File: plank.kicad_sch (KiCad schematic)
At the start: 14 parts, among them SW1 SW_Push, U1 ATmega32U4-A, Y1 16MHz

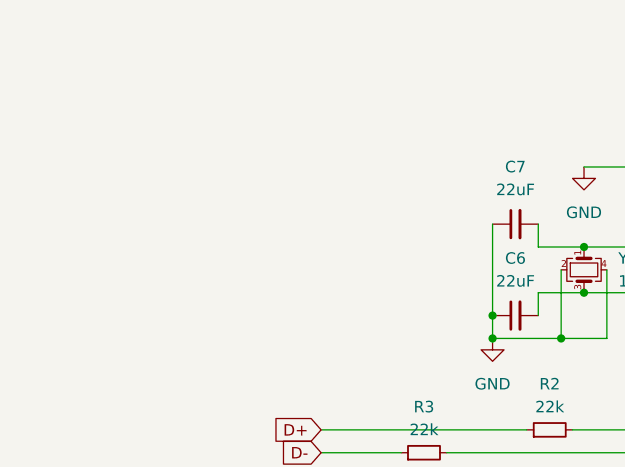
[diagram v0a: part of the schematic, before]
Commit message: Added USB Molex
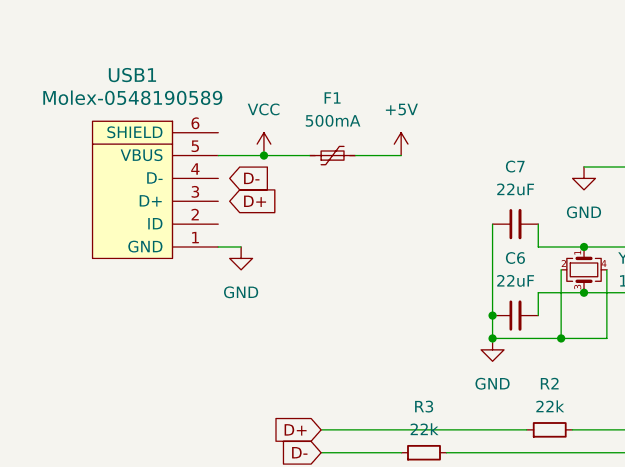
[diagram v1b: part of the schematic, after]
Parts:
- added F1: 500mA, symbol Device:Polyfuse_Small
- added USB1: Molex-0548190589, symbol random-keyboard-parts:Molex-0548190589
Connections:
- net +5V: now also F1.2
- net GND: now also USB1.1 (GND)
- new net VCC: F1.1, USB1.5 (VBUS)
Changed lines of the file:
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@@
   (junction (at 82.55 57.15) (diameter 0) (color 0 0 0 0)
+  )
+  (junction (at 57.15 39.37) (diameter 0) (color 0 0 0 0)
   )
   (junction (at 124.46 128.27) (diameter 0) (color 0 0 0 0)
@@
     (stroke (width 0) (type default))
   )
+  (wire (pts (xy 67.31 39.37) (xy 72.39 39.37))
+    (stroke (width 0) (type default))
+  )
   (wire (pts (xy 92.71 54.61) (xy 111.76 54.61))
     (stroke (width 0) (type default))
@@
     (stroke (width 0) (type default))
   )
+  (wire (pts (xy 52.07 49.53) (xy 54.61 49.53))
+    (stroke (width 0) (type default))
+  )
   (wire (pts (xy 99.06 40.64) (xy 92.71 40.64))
     (stroke (width 0) (type default))
@@
     (stroke (width 0) (type default))
   )
+  (wire (pts (xy 57.15 39.37) (xy 62.23 39.37))
+    (stroke (width 0) (type default))
+  )
   (wire (pts (xy 64.77 101.6) (xy 77.47 101.6))
     (stroke (width 0) (type default))
@@
   )
   (wire (pts (xy 90.17 106.68) (xy 102.87 106.68))
+    (stroke (width 0) (type default))
+  )
+  (wire (pts (xy 52.07 39.37) (xy 57.15 39.37))
     (stroke (width 0) (type default))
   )
@@
     )
   )
+  (global_label "D+" (shape input) (at 53.34 44.45 0) (fields_autoplaced)
+    (effects (font (size 1.27 1.27)) (justify left))
+    (property "Intersheetrefs" "${INTERSHEET_REFS}" (at 59.1676 44.45 0)
+      (effects (font (size 1.27 1.27)) (justify left) hide)
+    )
+  )
+  (global_label "D-" (shape input) (at 53.34 41.91 0) (fields_autoplaced)
+    (effects (font (size 1.27 1.27)) (justify left))
+    (property "Intersheetrefs" "${INTERSHEET_REFS}" (at 59.1676 41.91 0)
+      (effects (font (size 1.27 1.27)) (justify left) hide)
+    )
+  )
   (global_label "D-" (shape input) (at 63.5 72.39 180) (fields_autoplaced)
     (effects (font (size 1.27 1.27)) (justify right))
@@
     )
   )
+  (symbol (lib_id "power:+5V") (at 72.39 39.37 0) (unit 1)
+    (in_bom yes) (on_board yes) (dnp no) (fields_autoplaced)
+    (property "Reference" "#PWR012" (at 72.39 43.18 0)
+      (effects (font (size 1.27 1.27)) hide)
+    )
+    (property "Value" "+5V" (at 72.39 34.29 0)
+      (effects (font (size 1.27 1.27)))
+    )
+    (property "Footprint" "" (at 72.39 39.37 0)
+      (effects (font (size 1.27 1.27)) hide)
+    )
+    (property "Datasheet" "" (at 72.39 39.37 0)
+      (effects (font (size 1.27 1.27)) hide)
+    )
+    (pin "1")
+    (instances
+      (project "plank"
+        (path "/56e11f07-968c-4d42-931a-9a646d695afe"
+          (reference "#PWR012") (unit 1)
+        )
+      )
+    )
+  )
   (symbol (lib_id "Device:C_Small") (at 77.47 104.14 0) (unit 1)
     (in_bom yes) (on_board yes) (dnp no) (fields_autoplaced)
@@
     )
   )
+  (symbol (lib_id "random-keyboard-parts:Molex-0548190589") (at 44.45 44.45 90) (unit 1)
+    (in_bom yes) (on_board yes) (dnp no) (fields_autoplaced)
+    (property "Reference" "USB1" (at 42.545 30.48 90)
+      (effects (font (size 1.524 1.524)))
+    )
+    (property "Value" "Molex-0548190589" (at 42.545 33.02 90)
+      (effects (font (size 1.524 1.524)))
+    )
+    (property "Footprint" "" (at 44.45 44.45 0)
+      (effects (font (size 1.524 1.524)) hide)
+    )
+    (property "Datasheet" "" (at 44.45 44.45 0)
+      (effects (font (size 1.524 1.524)) hide)
+    )
+    (pin "6")
+    (pin "1")
+    (pin "2")
+    (pin "3")
+    (pin "4")
+    (pin "5")
+    (instances
+      (project "plank"
+        (path "/56e11f07-968c-4d42-931a-9a646d695afe"
+          (reference "USB1") (unit 1)
+        )
+      )
+    )
+  )
   (symbol (lib_id "power:GND") (at 101.6 85.09 0) (unit 1)
     (in_bom yes) (on_board yes) (dnp no) (fields_autoplaced)
@@
     )
   )
+  (symbol (lib_id "power:VCC") (at 57.15 39.37 0) (unit 1)
+    (in_bom yes) (on_board yes) (dnp no) (fields_autoplaced)
+    (property "Reference" "#PWR011" (at 57.15 43.18 0)
+      (effects (font (size 1.27 1.27)) hide)
+    )
+    (property "Value" "VCC" (at 57.15 34.29 0)
+      (effects (font (size 1.27 1.27)))
+    )
+    (property "Footprint" "" (at 57.15 39.37 0)
+      (effects (font (size 1.27 1.27)) hide)
+    )
+    (property "Datasheet" "" (at 57.15 39.37 0)
+      (effects (font (size 1.27 1.27)) hide)
+    )
+    (pin "1")
+    (instances
+      (project "plank"
+        (path "/56e11f07-968c-4d42-931a-9a646d695afe"
+          (reference "#PWR011") (unit 1)
+        )
+      )
+    )
+  )
   (symbol (lib_id "Device:R_Small") (at 110.49 35.56 0) (unit 1)
     (in_bom yes) (on_board yes) (dnp no) (fields_autoplaced)
@@
         (path "/56e11f07-968c-4d42-931a-9a646d695afe"
           (reference "R4") (unit 1)
+        )
+      )
+    )
+  )
+  (symbol (lib_id "power:GND") (at 54.61 49.53 0) (unit 1)
+    (in_bom yes) (on_board yes) (dnp no) (fields_autoplaced)
+    (property "Reference" "#PWR013" (at 54.61 55.88 0)
+      (effects (font (size 1.27 1.27)) hide)
+    )
+    (property "Value" "GND" (at 54.61 54.61 0)
+      (effects (font (size 1.27 1.27)))
+    )
+    (property "Footprint" "" (at 54.61 49.53 0)
+      (effects (font (size 1.27 1.27)) hide)
+    )
+    (property "Datasheet" "" (at 54.61 49.53 0)
+      (effects (font (size 1.27 1.27)) hide)
+    )
+    (pin "1")
+    (instances
+      (project "plank"
+        (path "/56e11f07-968c-4d42-931a-9a646d695afe"
+          (reference "#PWR013") (unit 1)
         )
       )
@@
         )
       )
+    )
+  )
+  (symbol (lib_id "Device:Polyfuse_Small") (at 64.77 39.37 90) (unit 1)
+    (in_bom yes) (on_board yes) (dnp no) (fields_autoplaced)
+    (property "Reference" "F1" (at 64.77 33.02 90)
+      (effects (font (size 1.27 1.27)))
+    )
+    (property "Value" "500mA" (at 64.77 35.56 90)
+      (effects (font (size 1.27 1.27)))
+    )
+    (property "Footprint" "" (at 69.85 38.1 0)
+      (effects (font (size 1.27 1.27)) (justify left) hide)
+    )
+    (property "Datasheet" "~" (at 64.77 39.37 0)
+      (effects (font (size 1.27 1.27)) hide)
+    )
+    (pin "2")
+    (pin "1")
+    (instances
+      (project "plank"
+        (path "/56e11f07-968c-4d42-931a-9a646d695afe"
+          (reference "F1") (unit 1)
+        )
+      )

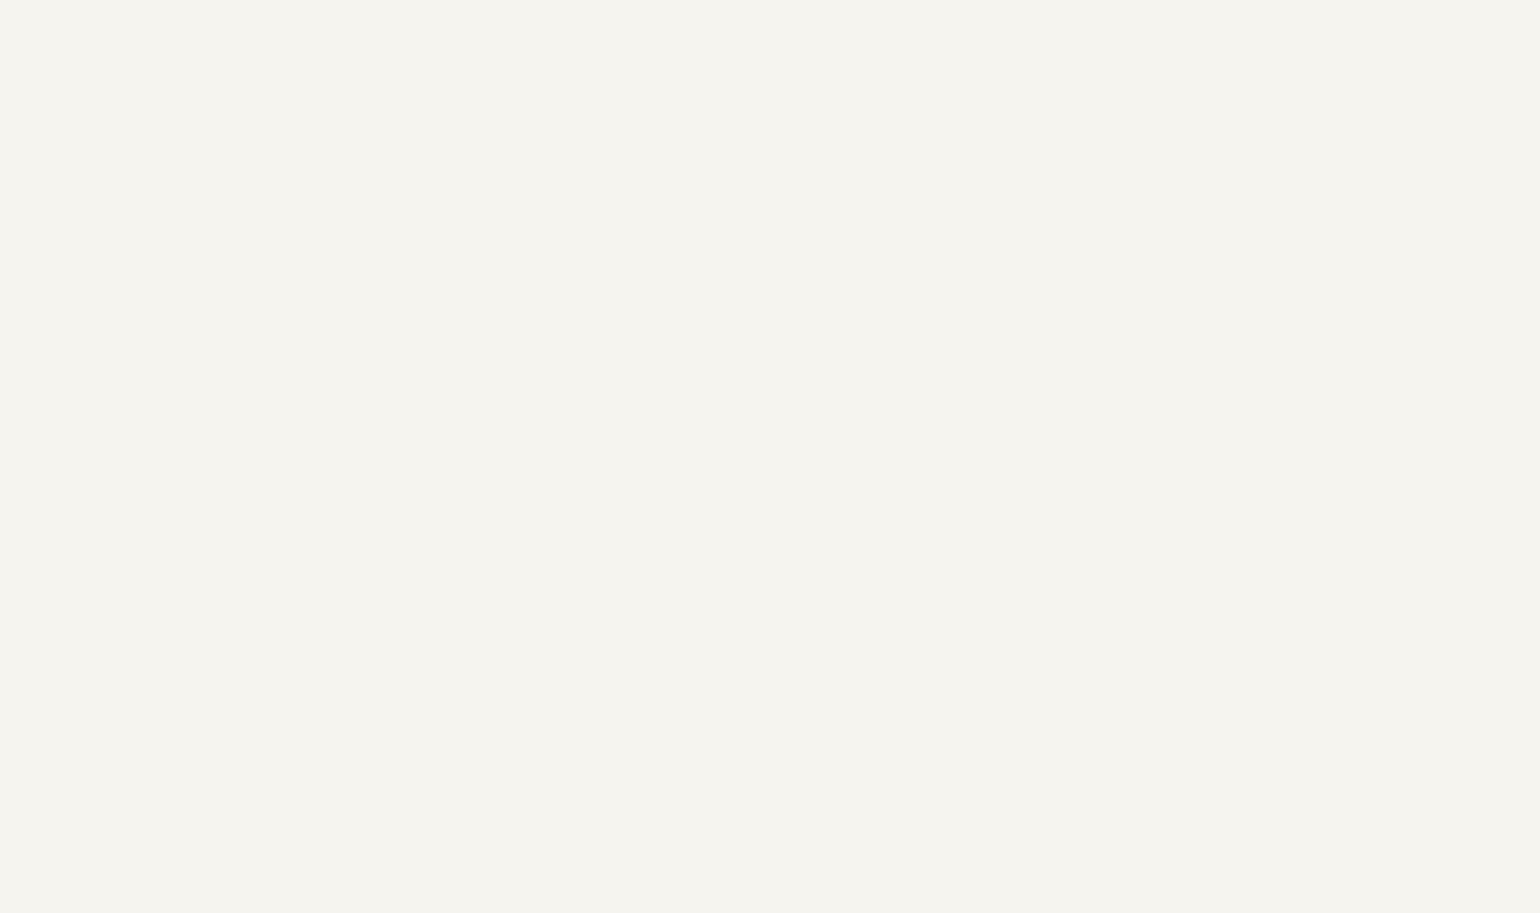
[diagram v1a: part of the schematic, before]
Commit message: Added switch matrix
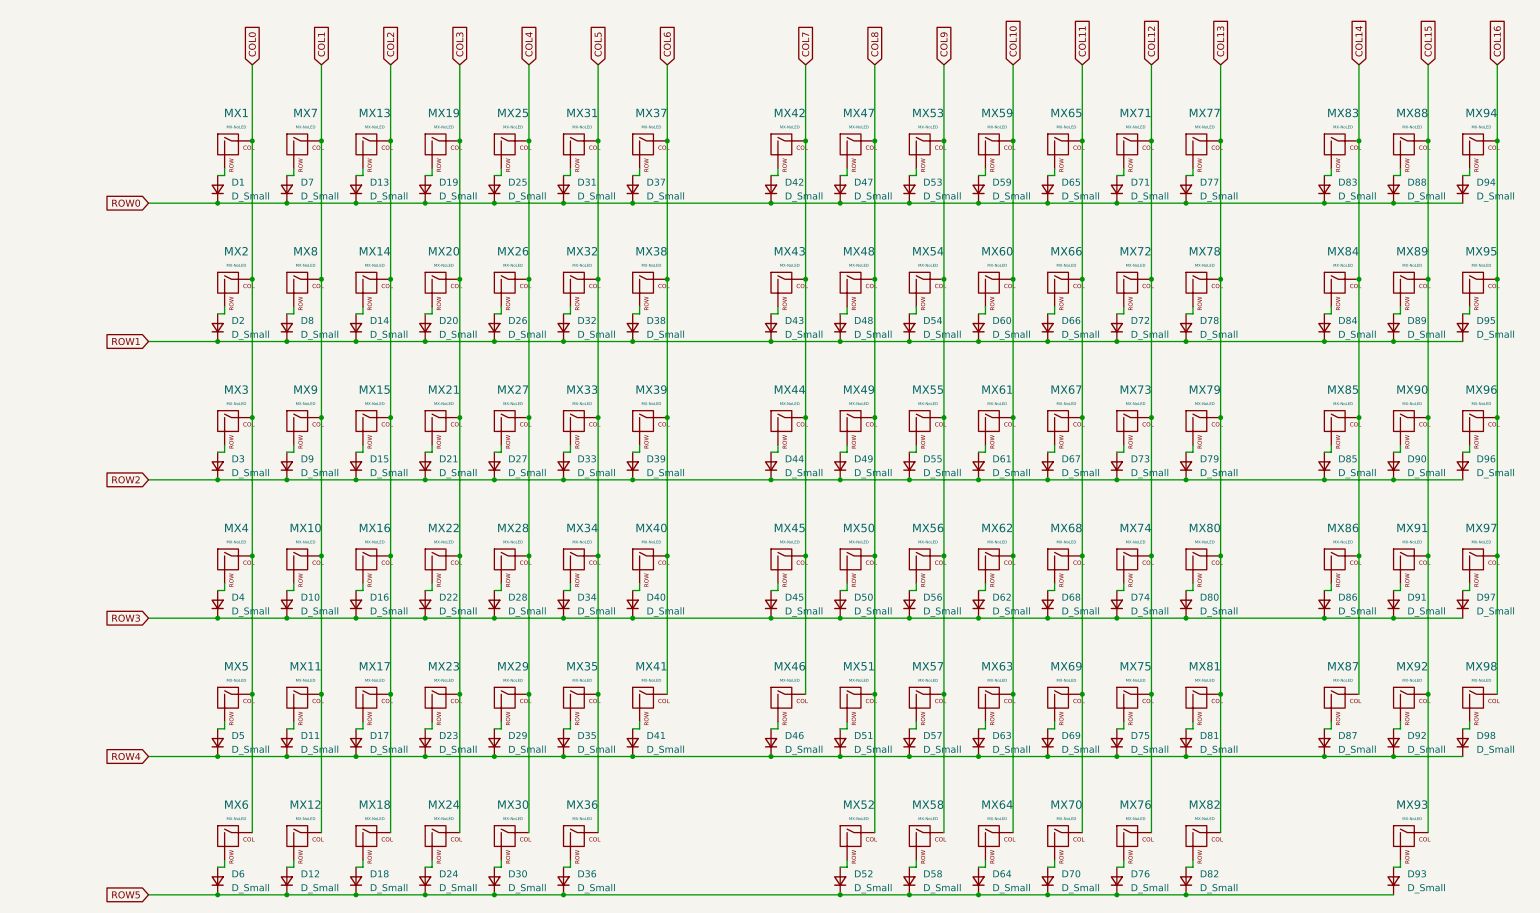
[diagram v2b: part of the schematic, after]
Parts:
- added D1, D10, D11, D12, D13, D14, D15, D16, D17, D18, D19, D2, D20, D21, D22, D23, D24, D25, D26, D27, D28, D29, D3, D30, D31, D32, D33, D34, D35, D36, D37, D38, D39, D4, D40, D41, D42, D43, D44, D45, D46, D47, D48, D49, D5, D50, D51, D52, D53, D54, D55, D56, D57, D58, D59, D6, D60, D61, D62, D63, D64, D65, D66, D67, D68, D69, D7, D70, D71, D72, D73, D74, D75, D76, D77, D78, D79, D8, D80, D81, D82, D83, D84, D85, D86, D87, D88, D89, D9, D90, D91, D92, D93, D94, D95, D96, D97, D98: D_Small, symbol Device:D_Small
- added MX1, MX10, MX11, MX12, MX13, MX14, MX15, MX16, MX17, MX18, MX19, MX2, MX20, MX21, MX22, MX23, MX24, MX25, MX26, MX27, MX28, MX29, MX3, MX30, MX31, MX32, MX33, MX34, MX35, MX36, MX37, MX38, MX39, MX4, MX40, MX41, MX42, MX43, MX44, MX45, MX46, MX47, MX48, MX49, MX5, MX50, MX51, MX52, MX53, MX54, MX55, MX56, MX57, MX58, MX59, MX6, MX60, MX61, MX62, MX63, MX64, MX65, MX66, MX67, MX68, MX69, MX7, MX70, MX71, MX72, MX73, MX74, MX75, MX76, MX77, MX78, MX79, MX8, MX80, MX81, MX82, MX83, MX84, MX85, MX86, MX87, MX88, MX89, MX9, MX90, MX91, MX92, MX93, MX94, MX95, MX96, MX97, MX98: MX-NoLED, symbol MX_Alps_Hybrid:MX-NoLED
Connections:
- new net: D26.2 (A), MX26.2 (ROW)
- new net: D72.2 (A), MX72.2 (ROW)
- new net: D75.2 (A), MX75.2 (ROW)
- new net: D35.2 (A), MX35.2 (ROW)
- new net: D70.2 (A), MX70.2 (ROW)
- new net: D5.2 (A), MX5.2 (ROW)
- new net: D32.2 (A), MX32.2 (ROW)
- new net: D29.2 (A), MX29.2 (ROW)
- new net: D3.2 (A), MX3.2 (ROW)
- new net: D74.2 (A), MX74.2 (ROW)
- new net: D45.2 (A), MX45.2 (ROW)
- new net: D39.2 (A), MX39.2 (ROW)
- new net: D47.2 (A), MX47.2 (ROW)
- new net: D44.2 (A), MX44.2 (ROW)
- new net: D20.2 (A), MX20.2 (ROW)
- new net: D58.2 (A), MX58.2 (ROW)
- new net: D55.2 (A), MX55.2 (ROW)
- new net: D84.2 (A), MX84.2 (ROW)
- new net: D77.2 (A), MX77.2 (ROW)
- new net: D13.2 (A), MX13.2 (ROW)
- new net: D15.2 (A), MX15.2 (ROW)
- new net: D79.2 (A), MX79.2 (ROW)
- new net: D63.2 (A), MX63.2 (ROW)
- new net: D18.2 (A), MX18.2 (ROW)
- new net: D95.2 (A), MX95.2 (ROW)
- new net: D80.2 (A), MX80.2 (ROW)
- new net: D21.2 (A), MX21.2 (ROW)
- new net: D66.2 (A), MX66.2 (ROW)
- new net: D91.2 (A), MX91.2 (ROW)
- new net: D98.2 (A), MX98.2 (ROW)
- new net: D33.2 (A), MX33.2 (ROW)
- new net: D82.2 (A), MX82.2 (ROW)
- new net: D59.2 (A), MX59.2 (ROW)
- new net: D62.2 (A), MX62.2 (ROW)
- new net: D50.2 (A), MX50.2 (ROW)
- new net: D31.2 (A), MX31.2 (ROW)
- new net: D83.2 (A), MX83.2 (ROW)
- new net: D52.2 (A), MX52.2 (ROW)
- new net: D12.2 (A), MX12.2 (ROW)
- new net: D49.2 (A), MX49.2 (ROW)
- new net: D81.2 (A), MX81.2 (ROW)
- new net: D53.2 (A), MX53.2 (ROW)
- new net: D19.2 (A), MX19.2 (ROW)
- new net: D4.2 (A), MX4.2 (ROW)
- new net: D89.2 (A), MX89.2 (ROW)
- new net: D92.2 (A), MX92.2 (ROW)
- new net: D96.2 (A), MX96.2 (ROW)
- new net: D67.2 (A), MX67.2 (ROW)
- new net: D14.2 (A), MX14.2 (ROW)
- new net: D90.2 (A), MX90.2 (ROW)
- new net: D24.2 (A), MX24.2 (ROW)
- new net: D54.2 (A), MX54.2 (ROW)
- new net: D34.2 (A), MX34.2 (ROW)
- new net: D7.2 (A), MX7.2 (ROW)
- new net: D11.2 (A), MX11.2 (ROW)
- new net: D37.2 (A), MX37.2 (ROW)
- new net: D42.2 (A), MX42.2 (ROW)
- new net: D23.2 (A), MX23.2 (ROW)
- new net: D36.2 (A), MX36.2 (ROW)
- new net: D97.2 (A), MX97.2 (ROW)
- new net: D51.2 (A), MX51.2 (ROW)
- new net: D25.2 (A), MX25.2 (ROW)
- new net: D86.2 (A), MX86.2 (ROW)
- new net: D17.2 (A), MX17.2 (ROW)
- new net: D30.2 (A), MX30.2 (ROW)
- new net: D28.2 (A), MX28.2 (ROW)
- new net: D46.2 (A), MX46.2 (ROW)
- new net: D94.2 (A), MX94.2 (ROW)
- new net: D57.2 (A), MX57.2 (ROW)
- new net: D88.2 (A), MX88.2 (ROW)
- new net: D27.2 (A), MX27.2 (ROW)
- new net: D48.2 (A), MX48.2 (ROW)
- new net: D9.2 (A), MX9.2 (ROW)
- new net: D64.2 (A), MX64.2 (ROW)
- new net: D8.2 (A), MX8.2 (ROW)
- new net: D73.2 (A), MX73.2 (ROW)
- new net: D76.2 (A), MX76.2 (ROW)
- new net: D6.2 (A), MX6.2 (ROW)
- new net: D2.2 (A), MX2.2 (ROW)
- new net: D38.2 (A), MX38.2 (ROW)
- new net: D10.2 (A), MX10.2 (ROW)
- new net: D65.2 (A), MX65.2 (ROW)
- new net: D71.2 (A), MX71.2 (ROW)
- new net: D60.2 (A), MX60.2 (ROW)
- new net: D61.2 (A), MX61.2 (ROW)
- new net: D43.2 (A), MX43.2 (ROW)
- new net: D69.2 (A), MX69.2 (ROW)
- new net: D87.2 (A), MX87.2 (ROW)
- new net: D93.2 (A), MX93.2 (ROW)
- new net: D41.2 (A), MX41.2 (ROW)
- new net: D22.2 (A), MX22.2 (ROW)
- new net: D78.2 (A), MX78.2 (ROW)
- new net: D1.2 (A), MX1.2 (ROW)
- new net: D40.2 (A), MX40.2 (ROW)
- new net: D56.2 (A), MX56.2 (ROW)
- new net: D68.2 (A), MX68.2 (ROW)
- new net: D85.2 (A), MX85.2 (ROW)
- new net: D16.2 (A), MX16.2 (ROW)
- new net COL0: MX1.1 (COL), MX2.1 (COL), MX3.1 (COL), MX4.1 (COL), MX5.1 (COL), MX6.1 (COL)
- new net COL1: MX10.1 (COL), MX11.1 (COL), MX12.1 (COL), MX7.1 (COL), MX8.1 (COL), MX9.1 (COL)
- new net COL10: MX59.1 (COL), MX60.1 (COL), MX61.1 (COL), MX62.1 (COL), MX63.1 (COL), MX64.1 (COL)
- new net COL11: MX65.1 (COL), MX66.1 (COL), MX67.1 (COL), MX68.1 (COL), MX69.1 (COL), MX70.1 (COL)
- new net COL12: MX71.1 (COL), MX72.1 (COL), MX73.1 (COL), MX74.1 (COL), MX75.1 (COL), MX76.1 (COL)
- new net COL13: MX77.1 (COL), MX78.1 (COL), MX79.1 (COL), MX80.1 (COL), MX81.1 (COL), MX82.1 (COL)
- new net COL14: MX83.1 (COL), MX84.1 (COL), MX85.1 (COL), MX86.1 (COL), MX87.1 (COL)
- new net COL15: MX88.1 (COL), MX89.1 (COL), MX90.1 (COL), MX91.1 (COL), MX92.1 (COL), MX93.1 (COL)
- new net COL16: MX94.1 (COL), MX95.1 (COL), MX96.1 (COL), MX97.1 (COL), MX98.1 (COL)
- new net COL2: MX13.1 (COL), MX14.1 (COL), MX15.1 (COL), MX16.1 (COL), MX17.1 (COL), MX18.1 (COL)
- new net COL3: MX19.1 (COL), MX20.1 (COL), MX21.1 (COL), MX22.1 (COL), MX23.1 (COL), MX24.1 (COL)
- new net COL4: MX25.1 (COL), MX26.1 (COL), MX27.1 (COL), MX28.1 (COL), MX29.1 (COL), MX30.1 (COL)
- new net COL5: MX31.1 (COL), MX32.1 (COL), MX33.1 (COL), MX34.1 (COL), MX35.1 (COL), MX36.1 (COL)
- new net COL6: MX37.1 (COL), MX38.1 (COL), MX39.1 (COL), MX40.1 (COL), MX41.1 (COL)
- new net COL7: MX42.1 (COL), MX43.1 (COL), MX44.1 (COL), MX45.1 (COL), MX46.1 (COL)
- new net COL8: MX47.1 (COL), MX48.1 (COL), MX49.1 (COL), MX50.1 (COL), MX51.1 (COL), MX52.1 (COL)
- new net COL9: MX53.1 (COL), MX54.1 (COL), MX55.1 (COL), MX56.1 (COL), MX57.1 (COL), MX58.1 (COL)
- new net ROW0: D1.1 (K), D13.1 (K), D19.1 (K), D25.1 (K), D31.1 (K), D37.1 (K), D42.1 (K), D47.1 (K), D53.1 (K), D59.1 (K), D65.1 (K), D7.1 (K), D71.1 (K), D77.1 (K), D83.1 (K), D88.1 (K), D94.1 (K)
- new net ROW1: D14.1 (K), D2.1 (K), D20.1 (K), D26.1 (K), D32.1 (K), D38.1 (K), D43.1 (K), D48.1 (K), D54.1 (K), D60.1 (K), D66.1 (K), D72.1 (K), D78.1 (K), D8.1 (K), D84.1 (K), D89.1 (K), D95.1 (K)
- new net ROW2: D15.1 (K), D21.1 (K), D27.1 (K), D3.1 (K), D33.1 (K), D39.1 (K), D44.1 (K), D49.1 (K), D55.1 (K), D61.1 (K), D67.1 (K), D73.1 (K), D79.1 (K), D85.1 (K), D9.1 (K), D90.1 (K), D96.1 (K)
- new net ROW3: D10.1 (K), D16.1 (K), D22.1 (K), D28.1 (K), D34.1 (K), D4.1 (K), D40.1 (K), D45.1 (K), D50.1 (K), D56.1 (K), D62.1 (K), D68.1 (K), D74.1 (K), D80.1 (K), D86.1 (K), D91.1 (K), D97.1 (K)
- new net ROW4: D11.1 (K), D17.1 (K), D23.1 (K), D29.1 (K), D35.1 (K), D41.1 (K), D46.1 (K), D5.1 (K), D51.1 (K), D57.1 (K), D63.1 (K), D69.1 (K), D75.1 (K), D81.1 (K), D87.1 (K), D92.1 (K), D98.1 (K)
- new net ROW5: D12.1 (K), D18.1 (K), D24.1 (K), D30.1 (K), D36.1 (K), D52.1 (K), D58.1 (K), D6.1 (K), D64.1 (K), D70.1 (K), D76.1 (K), D82.1 (K), D93.1 (K)

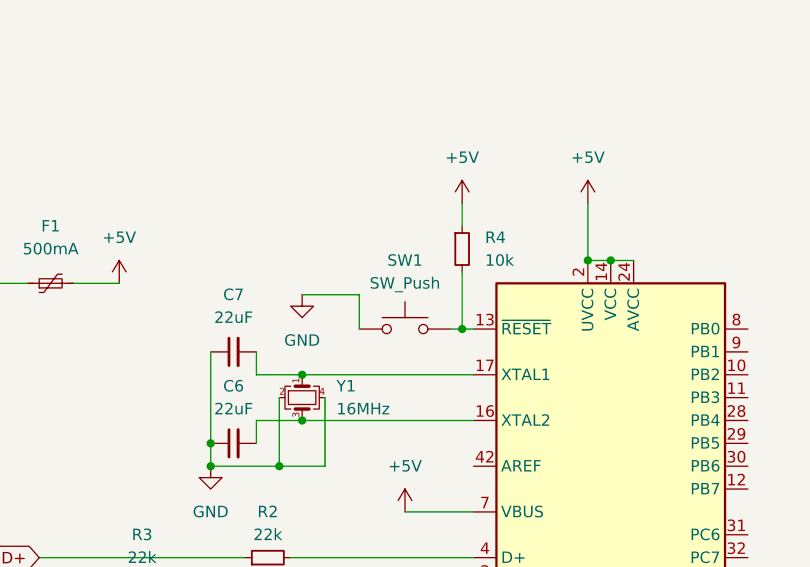
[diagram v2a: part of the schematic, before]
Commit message: Started the PCB layout
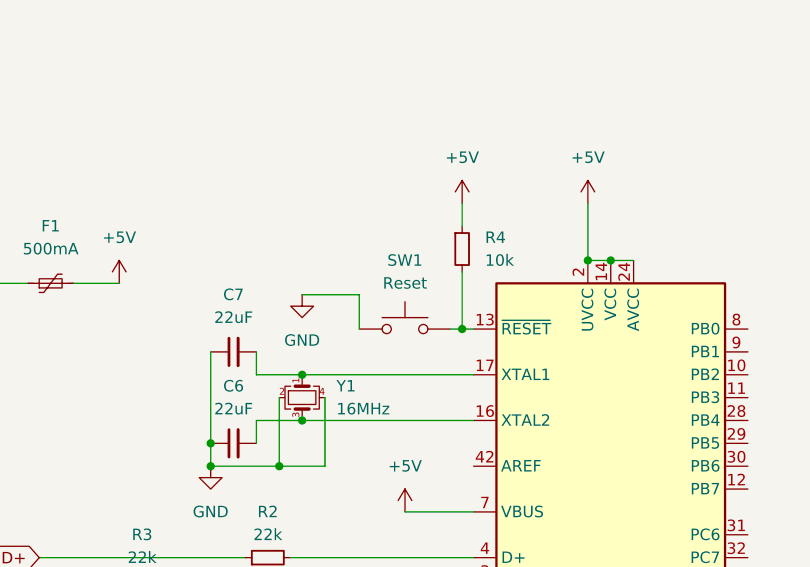
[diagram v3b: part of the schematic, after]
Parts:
- C1, C2, C3, C4, C5, C6, C7: footprint (none) -> Capacitor_SMD:C_0805_2012Metric
- D1, D10, D11, D12, D13, D14, D15, D16, D17, D18, D19, D2, D20, D21, D22, D23, D24, D25, D26, D27, D28, D29, D3, D30, D31, D32, D33, D34, D35, D36, D37, D38, D39, D4, D40, D41, D42, D43, D44, D45, D46, D47, D48, D49, D5, D50, D51, D52, D53, D54, D55, D56, D57, D58, D59, D6, D60, D61, D62, D63, D64, D65, D66, D67, D68, D69, D7, D70, D71, D72, D73, D74, D75, D76, D77, D78, D79, D8, D80, D81, D82, D83, D84, D85, D86, D87, D88, D89, D9, D90, D91, D92, D93, D94, D95, D96, D97, D98: footprint (none) -> Diode_SMD:D_SOD-123
- F1: footprint (none) -> Fuse:Fuse_1206_3216Metric
- MX1, MX10, MX11, MX12, MX13, MX14, MX15, MX16, MX17, MX18, MX19, MX2, MX20, MX21, MX22, MX23, MX24, MX25, MX26, MX27, MX28, MX29, MX3, MX30, MX31, MX32, MX33, MX34, MX35, MX36, MX37, MX38, MX39, MX4, MX40, MX41, MX42, MX43, MX44, MX45, MX46, MX47, MX48, MX49, MX5, MX50, MX51, MX52, MX53, MX54, MX55, MX56, MX57, MX58, MX59, MX6, MX60, MX61, MX62, MX63, MX64, MX65, MX66, MX67, MX68, MX69, MX7, MX70, MX71, MX72, MX73, MX74, MX75, MX76, MX77, MX78, MX79, MX8, MX80, MX81, MX82, MX83, MX84, MX85, MX86, MX87, MX88, MX89, MX9, MX90, MX91, MX92, MX93, MX94, MX95, MX96, MX97, MX98: footprint (none) -> Button_Switch_Keyboard:SW_Cherry_MX_1.00u_PCB
- R1, R2, R3, R4: footprint (none) -> Resistor_SMD:R_0805_2012Metric
- SW1: value SW_Push -> Reset; footprint (none) -> Button_Switch_SMD:Panasonic_EVQPUJ_EVQPUA
- USB1: footprint (none) -> Connector_Molex:Molex_SL_171971-0006_1x06_P2.54mm_Vertical
- Y1: footprint (none) -> Crystal:Crystal_SMD_3225-4Pin_3.2x2.5mm
